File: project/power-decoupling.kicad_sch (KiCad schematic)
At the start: 101 parts, among them IC2 STPMIC1DPQR, IC3 MAX17262REWL+T, IC4 LD39200PU33R, IC5 TPS2117DRLR, SW1 PTS636SM43SMTR LFS, U2 MCP73831-2-OT

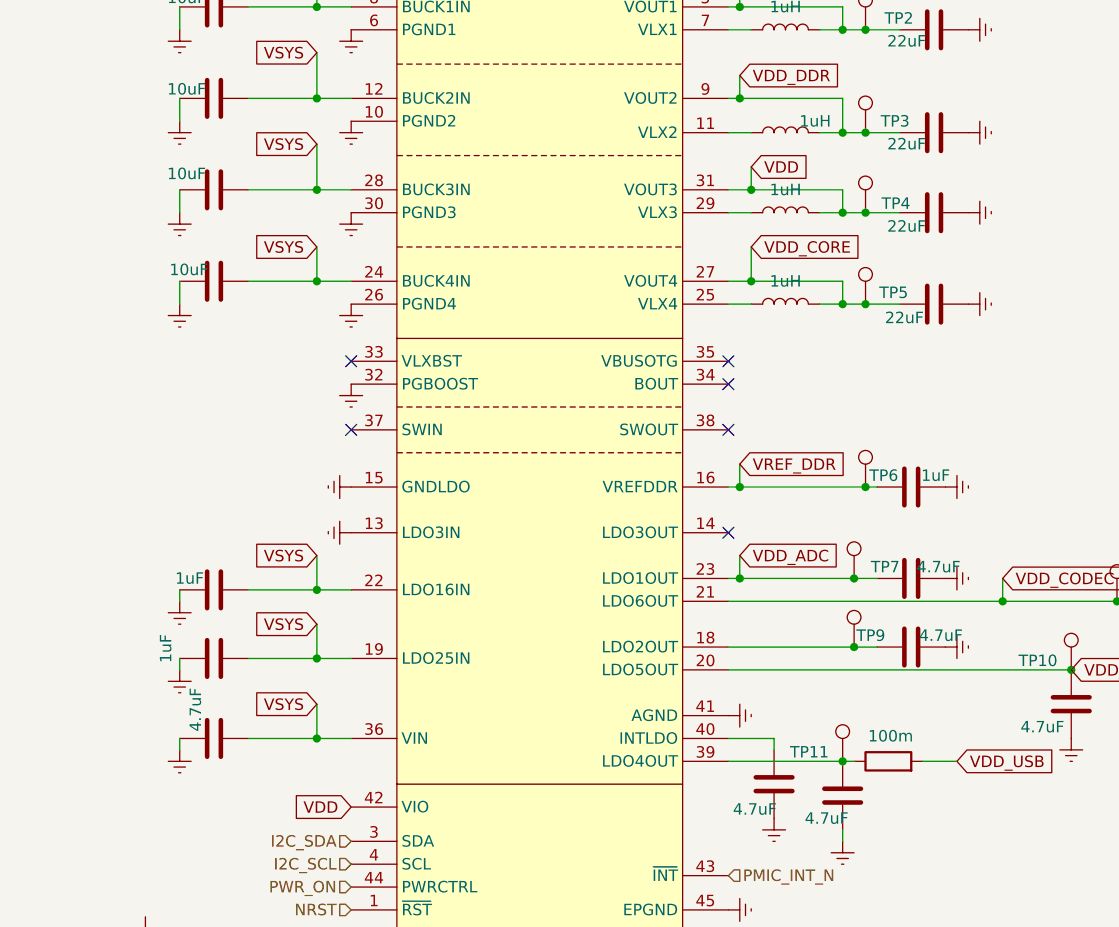
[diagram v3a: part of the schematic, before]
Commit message: PCB design, finished RAM, audio, battery fuel gauge and charger, PMIC, USB C power
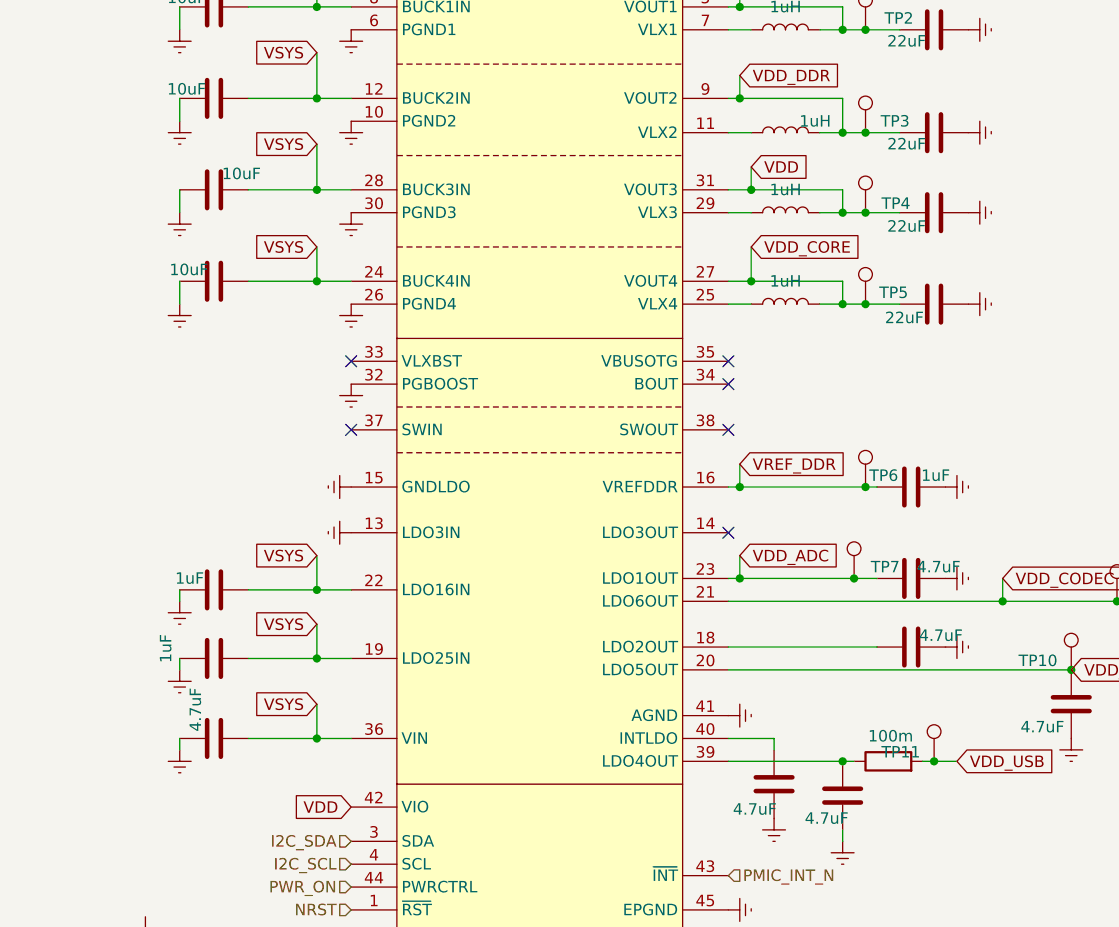
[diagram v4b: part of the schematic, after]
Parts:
- removed TP9: TestPoint, TestPoint:TestPoint_Pad_D1.0mm, symbol Connector:TestPoint
- IC3: footprint BGA9C40P3X3_147X145X69 -> bozi:BGA9C40P3X3_147X145X69_edit
- IC4: footprint SON95P300X300X100-7N-D -> bozi:SON95P300X300X100-7N-D_edit
- IC5: footprint SOTFL50P160X60-8N -> bozi:SOTFL50P160X60-8N_edit
- TH1: footprint bozi:THRMC1005X55N -> bozi:THRMC1005X55N_edit
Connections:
- net GND is gone; now on net GNDREF: BT1.2 (-), C78.2, C79.2, C82.2, IC3.C3 (GND), R17.2, TH1.2, U2.2 (V_{SS})
- net GNDREF: now also C44.1; no longer C44.2
- net VDD_USB: now also TP11.1
- net VSYS: now also C44.2; no longer C44.1
- net at C76.1, IC2.39 (LDO4OUT), R10.1: no longer TP11.1
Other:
- moved on the sheet: TP11
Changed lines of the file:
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@@
 	)
 	(junction
-		(at 358.14 104.14)
-		(diameter 0)
-		(color 0 0 0 0)
-	)
-	(junction
 		(at 57.15 63.5)
 		(diameter 0)
@@
 	)
 	(junction
+		(at 367.03 116.84)
+		(diameter 0)
+		(color 0 0 0 0)
+	)
+	(junction
 		(at 66.04 80.01)
 		(diameter 0)
@@
 	(wire
 		(pts
-			(xy 344.17 104.14) (xy 358.14 104.14)
-		)
-		(stroke
-			(width 0)
-			(type default)
-		)
-	)
-	(wire
-		(pts
 			(xy 43.18 185.42) (xy 48.26 185.42)
 		)
@@
 	(wire
 		(pts
-			(xy 365.76 116.84) (xy 369.57 116.84)
+			(xy 365.76 116.84) (xy 367.03 116.84)
 		)
 		(stroke
@@
 	(wire
 		(pts
-			(xy 360.68 104.14) (xy 358.14 104.14)
+			(xy 344.17 104.14) (xy 360.68 104.14)
 		)
 		(stroke
@@
 	(wire
 		(pts
+			(xy 367.03 116.84) (xy 369.57 116.84)
+		)
+		(stroke
+			(width 0)
+			(type default)
+		)
+	)
+	(wire
+		(pts
 			(xy 359.41 35.56) (xy 356.87 35.56)
 		)
@@
 			)
 		)
-		(property "Value" "GND"
+		(property "Value" "GNDREF"
 			(at 90.17 213.36 0)
 			(effects
@@
 	(symbol
 		(lib_id "Connector:TestPoint")
-		(at 356.87 116.84 0)
+		(at 367.03 116.84 0)
 		(unit 1)
 		(exclude_from_sim no)
@@
 		(dnp no)
 		(property "Reference" "TP11"
-			(at 355.346 115.824 0)
+			(at 365.506 115.824 0)
 			(effects
 				(font
@@
 		)
 		(property "Value" "TestPoint"
-			(at 354.33 114.8079 0)
+			(at 364.49 114.8079 0)
 			(effects
 				(font
@@
 		)
 		(property "Footprint" "TestPoint:TestPoint_Pad_D1.0mm"
-			(at 361.95 116.84 0)
+			(at 372.11 116.84 0)
 			(effects
 				(font
@@
 		)
 		(property "Datasheet" "~"
-			(at 361.95 116.84 0)
+			(at 372.11 116.84 0)
 			(effects
 				(font
@@
 		)
 		(property "Description" "test point"
-			(at 356.87 116.84 0)
+			(at 367.03 116.84 0)
 			(effects
 				(font
@@
 		)
 		(property "DigiKey_Part_Number" ""
-			(at 356.87 116.84 0)
+			(at 367.03 116.84 0)
 			(effects
 				(font
@@
 		)
 		(property "Availability" ""
-			(at 356.87 116.84 0)
+			(at 367.03 116.84 0)
 			(effects
 				(font
@@
 		)
 		(property "MAXIMUM_PACKAGE_HEIGHT" ""
-			(at 356.87 116.84 0)
+			(at 367.03 116.84 0)
 			(effects
 				(font
@@
 		)
 		(property "MF" ""
-			(at 356.87 116.84 0)
+			(at 367.03 116.84 0)
 			(effects
 				(font
@@
 		)
 		(property "MP" ""
-			(at 356.87 116.84 0)
+			(at 367.03 116.84 0)
 			(effects
 				(font
@@
 		)
 		(property "PARTREV" ""
-			(at 356.87 116.84 0)
+			(at 367.03 116.84 0)
 			(effects
 				(font
@@
 		)
 		(property "Package" ""
-			(at 356.87 116.84 0)
+			(at 367.03 116.84 0)
 			(effects
 				(font
@@
 		)
 		(property "Price" ""
-			(at 356.87 116.84 0)
+			(at 367.03 116.84 0)
 			(effects
 				(font
@@
 		)
 		(property "STANDARD" ""
-			(at 356.87 116.84 0)
+			(at 367.03 116.84 0)
 			(effects
 				(font
@@
 		)
 		(property "Type" ""
-			(at 356.87 116.84 0)
+			(at 367.03 116.84 0)
 			(effects
 				(font
@@
 		)
 		(property "3DMODEL" ""
-			(at 356.87 116.84 0)
+			(at 367.03 116.84 0)
 			(effects
 				(font
@@
 			)
 		)
-		(property "Value" "GND"
+		(property "Value" "GNDREF"
 			(at 171.45 214.63 0)
 			(effects
@@
 			)
 		)
-		(property "Value" "GND"
+		(property "Value" "GNDREF"
 			(at 113.03 213.36 0)
 			(effects
@@
 			)
 		)
-		(property "Footprint" "SOTFL50P160X60-8N"
+		(property "Footprint" "bozi:SOTFL50P160X60-8N_edit"
 			(at 121.92 350.19 0)
 			(effects
@@
 			)
 		)
-		(property "Value" "GND"
+		(property "Value" "GNDREF"
 			(at 48.26 213.36 0)
 			(effects
@@
 			)
 		)
-		(property "Value" "GND"
+		(property "Value" "GNDREF"
 			(at 101.6 213.36 0)
 			(effects
@@
 			)
 		)
-		(property "Footprint" "SON95P300X300X100-7N-D"
+		(property "Footprint" "bozi:SON95P300X300X100-7N-D_edit"
 			(at 354.33 289.23 0)
 			(effects
@@
 			)
 		)
-		(property "Value" "GND"
+		(property "Value" "GNDREF"
 			(at 137.16 208.28 0)
 			(effects
@@
 			)
 		)
-		(property "Footprint" "BGA9C40P3X3_147X145X69"
+		(property "Footprint" "bozi:BGA9C40P3X3_147X145X69_edit"
 			(at 166.37 289.23 0)
 			(effects
@@
 			)
 		)
-		(property "Footprint" "bozi:THRMC1005X55N"
+		(property "Footprint" "bozi:THRMC1005X55N_edit"
 			(at 137.16 193.04 0)
 			(effects
@@
 	)
 	(symbol
-		(lib_id "Connector:TestPoint")
-		(at 358.14 104.14 0)
-		(mirror y)
-		(unit 1)
-		(exclude_from_sim no)
-		(in_bom yes)
-		(on_board yes)
-		(dnp no)
-		(property "Reference" "TP9"
-			(at 358.394 102.87 0)
-			(effects
-				(font
-					(size 1.27 1.27)
-				)
-				(justify right)
-			)
-		)
-		(property "Value" "TestPoint"
-			(at 360.68 102.1079 0)
-			(effects
-				(font
-					(size 1.27 1.27)
-				)
-				(justify right)
-				(hide yes)
-			)
-		)
-		(property "Footprint" "TestPoint:TestPoint_Pad_D1.0mm"
-			(at 353.06 104.14 0)
-			(effects
-				(font
-					(size 1.27 1.27)
-				)
-				(hide yes)
-			)
-		)
-		(property "Datasheet" "~"
-			(at 353.06 104.14 0)
-			(effects
-				(font
-					(size 1.27 1.27)
-				)
-				(hide yes)
-			)
-		)
-		(property "Description" "test point"
-			(at 358.14 104.14 0)
-			(effects
-				(font
-					(size 1.27 1.27)
-				)
-				(hide yes)
-			)
-		)
-		(property "DigiKey_Part_Number" ""
-			(at 358.14 104.14 0)
-			(effects
-				(font
-					(size 1.27 1.27)
-				)
-				(hide yes)
-			)
-		)
-		(property "Availability" ""
-			(at 358.14 104.14 0)
-			(effects
-				(font
-					(size 1.27 1.27)
-				)
-				(hide yes)
-			)
-		)
-		(property "MAXIMUM_PACKAGE_HEIGHT" ""
-			(at 358.14 104.14 0)
-			(effects
-				(font
-					(size 1.27 1.27)
-				)
-				(hide yes)
-			)
-		)
-		(property "MF" ""
-			(at 358.14 104.14 0)
-			(effects
-				(font
-					(size 1.27 1.27)
-				)
-				(hide yes)
-			)
-		)
-		(property "MP" ""
-			(at 358.14 104.14 0)
-			(effects
-				(font
-					(size 1.27 1.27)
-				)
-				(hide yes)
-			)
-		)
-		(property "PARTREV" ""
-			(at 358.14 104.14 0)
-			(effects
-				(font
-					(size 1.27 1.27)
-				)
-				(hide yes)
-			)
-		)
-		(property "Package" ""
-			(at 358.14 104.14 0)
-			(effects
-				(font
-					(size 1.27 1.27)
-				)
-				(hide yes)
-			)
-		)
-		(property "Price" ""
-			(at 358.14 104.14 0)
-			(effects
-				(font
-					(size 1.27 1.27)
-				)
-				(hide yes)
-			)
-		)
-		(property "STANDARD" ""
-			(at 358.14 104.14 0)
-			(effects
-				(font
-					(size 1.27 1.27)
-				)
-				(hide yes)
-			)
-		)
-		(property "Type" ""
-			(at 358.14 104.14 0)
-			(effects
-				(font
-					(size 1.27 1.27)
-				)
-				(hide yes)
-			)
-		)
-		(property "3DMODEL" ""
-			(at 358.14 104.14 0)
-			(effects
-				(font
-					(size 1.27 1.27)
-				)
-				(hide yes)
-			)
-		)
-		(pin "1"
-		)
-		(instances
-			(project "project"
-				(path "/7afeae28-8837-445b-b53a-5d89eb16eb45/bb250b4f-c5d5-46d6-a17d-e2b7a9711818"
-					(reference "TP9")
-					(unit 1)
-				)
-			)
-		)
-	)
-	(symbol
 		(lib_id "Device:C")
 		(at 393.7 99.06 90)
@@
 	(symbol
 		(lib_id "Device:C")
-		(at 287.02 53.34 270)
+		(at 287.02 53.34 90)
+		(mirror x)
 		(unit 1)
 		(exclude_from_sim no)
@@
 		(dnp no)
 		(property "Reference" "C44"
-			(at 288.2901 57.15 0)
+			(at 285.7499 57.15 0)
 			(effects
 				(font
@@
 		)
 		(property "Value" "10uF"
-			(at 283.972 51.562 90)
+			(at 290.068 51.562 90)
 			(effects
 				(font
@@
 		)
 		(property "Footprint" "bozi:GRT18_T15"
-			(at 283.21 54.3052 0)
+			(at 290.83 54.3052 0)
 			(effects
 				(font
